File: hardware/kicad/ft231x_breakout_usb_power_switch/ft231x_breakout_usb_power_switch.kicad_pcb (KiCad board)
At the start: 2 copper layers, 60 x 31.2 mm, 48 parts, among them J1 USB_B_Micro_ALT, J2 USB_A_ALT, J4 Conn_01x04, SW1 PTS810SJK250SMTRLFS, U1 SRV05-4, U2 FT231XS, U3 TPS2553DBVR, U4 SN74LVC3G04DCTR, U5 NC7SZ66M5X

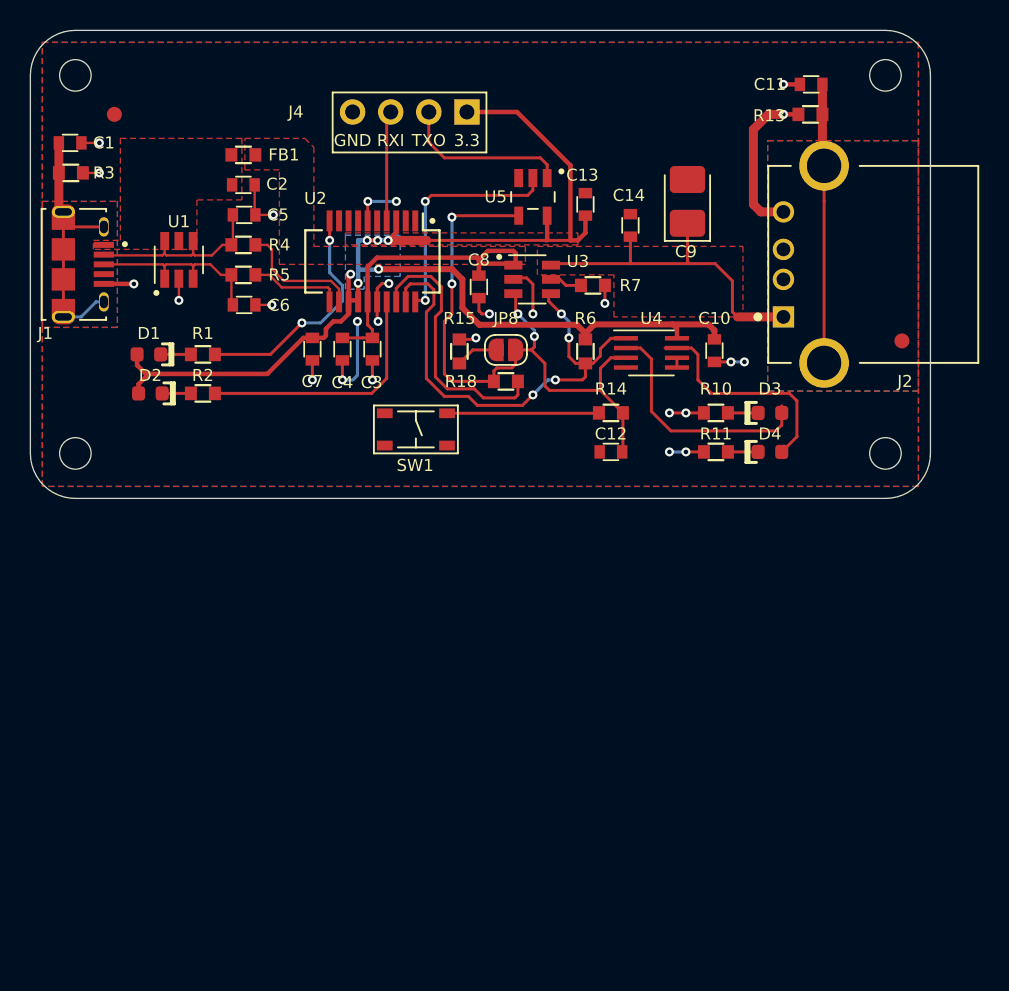
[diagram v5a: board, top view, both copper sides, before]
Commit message: 0.3-rc1 removed breakout headers
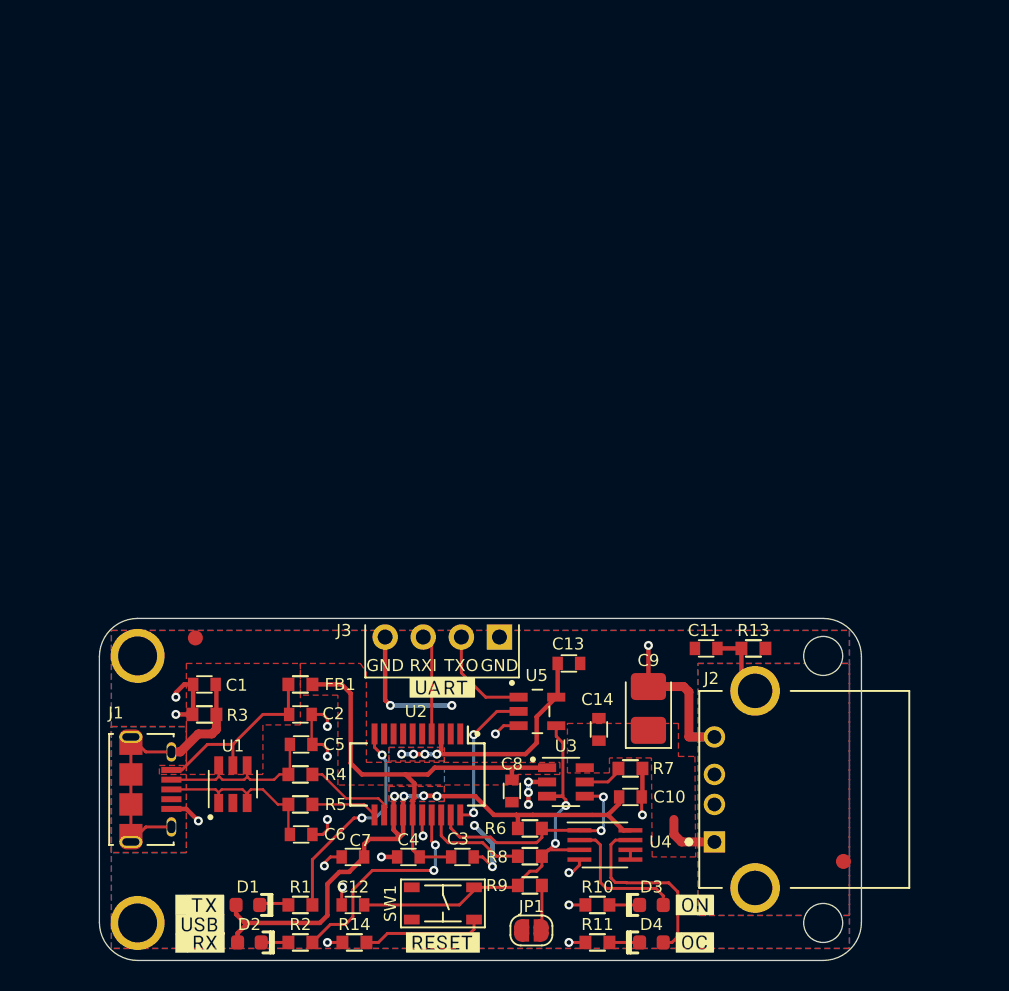
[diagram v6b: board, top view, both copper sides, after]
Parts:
- removed JP8: SolderJumper_2_Bridged_Alt, -Jumper:SolderJumper-2_P1.3mm_Un-Bridged_RoundedPad1.0x1.5mm
- removed R15: 10k, -Passive:R_0603
- removed R18: 5k1, -Passive:R_0603
- added ?: , buzzard_labels, F.Cu at (121.7, 130.2)
- added ?: , buzzard_labels, F.Cu at (121.7, 127.7)
- added ?: , buzzard_labels, F.Cu at (137.5, 130.2)
- added ?: , buzzard_labels, F.Cu at (137.5, 113.2)
- added ?: , buzzard_labels, F.Cu at (121.3, 129.0)
- added ?: , buzzard_labels, F.Cu at (154.3, 127.7)
- added ?: , buzzard_labels, F.Cu at (154.3, 130.2)
- added JP1: SolderJumper_2_Bridged_Alt, -Jumper:SolderJumper-2_P1.3mm_Un-Bridged_RoundedPad1.0x1.5mm, F.Cu at (143.4, 129.4)
- added R8: 5k1, -Passive:R_0603, F.Cu at (143.3, 124.5)
- added R9: 10k, -Passive:R_0603, F.Cu at (143.3, 126.4)
- H1, H3: footprint -Connector:MountingHole_2.1mm -> -Connector:MountingHole_2.6mm_annular
- H2, H4: footprint -Connector:MountingHole_2.1mm -> -Connector:MountingHole_2.6mm_nocrtyd
- moved R14 39.2 mm to (131.6, 130.2)
- moved H1 38.9 mm to (117.2, 111.1)
- moved H2 38.9 mm to (162.8, 111.1)
- moved C11 38.2 mm to (155.1, 110.6)
- moved D1 37.3 mm to (124.5, 127.7)
- moved R1 37.3 mm to (128.0, 127.7)
- moved C1 37.2 mm to (121.6, 113.0), turned to 180 degrees
- moved D2 37.2 mm to (124.6, 130.2)
- moved R3 37.2 mm to (121.6, 115.0), turned to 0 degrees
- moved R2 37.2 mm to (128.0, 130.2)
- moved R13 35.8 mm to (158.2, 110.6), turned to 180 degrees
- moved C2 35.5 mm to (128.0, 115.0)
- moved C5 35.5 mm to (128.1, 117.0)
- moved C6 35.5 mm to (128.1, 123.0)
- moved FB1 35.5 mm to (128.0, 113.0)
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- renumbered J4 to J3
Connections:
- J3 pad 1: +3V3 -> GND
- R14 pad 1: Net-(R14-Pad1) -> GND
- R14 pad 2: /EN -> Net-(R14-Pad2)
- SW1 pad 1: GND -> Net-(R14-Pad2)
- SW1 pad 3: Net-(R14-Pad1) -> /EN
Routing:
- net +3V3: track 88.0 -> 58.8 mm, vias 6 -> 8
- net Net-(C14-Pad1): track 23.9 -> 5.66 mm
- net /FAULT: track 32.2 -> 15.7 mm, vias 4 -> 2
- net /EN: track 42.4 -> 28.0 mm, vias 4 -> 2
- net Net-(C11-Pad1): track 18.6 -> 4.81 mm
- net Net-(C2-Pad1): track 0.00 -> 12.8 mm
- net /GPO: track 17.8 -> 7.06 mm
- net Net-(R14-Pad1): track 10.2 -> 0.00 mm
- net Net-(C3-Pad1): track 21.6 -> 29.9 mm
- net Net-(R14-Pad2): track 0.00 -> 8.26 mm
- net Net-(D3-Pad2): track 16.3 -> 10.1 mm
- net /TXD: track 15.6 -> 9.79 mm
- net GND: track 51.4 -> 57.0 mm, vias 26 -> 24
- net /STXD: track 11.4 -> 6.88 mm
- net Net-(JP1-Pad1): track 0.00 -> 3.32 mm
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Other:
- board size 60 x 31.2 mm -> 50.8 x 22.8 mm
- board text added: "Short JP1 to default USB power to off."
- board text added: "ft231x_uart_usb_power_switch"
- board text added: "v0.3<<hash>>"
- board text removed: "Short JP8 to default USB power to off."
- board text removed: "ft231x_breakout_usb_power_switch"
- board text removed: "v0.2<<hash>>"

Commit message: 0.3 rc2 fix zone fills
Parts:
- moved C11 0.10 mm to (155.1, 110.7)
- moved R13 0.10 mm to (158.2, 110.7)
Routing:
- net GND: track 57.0 -> 57.6 mm, vias 24 -> 25

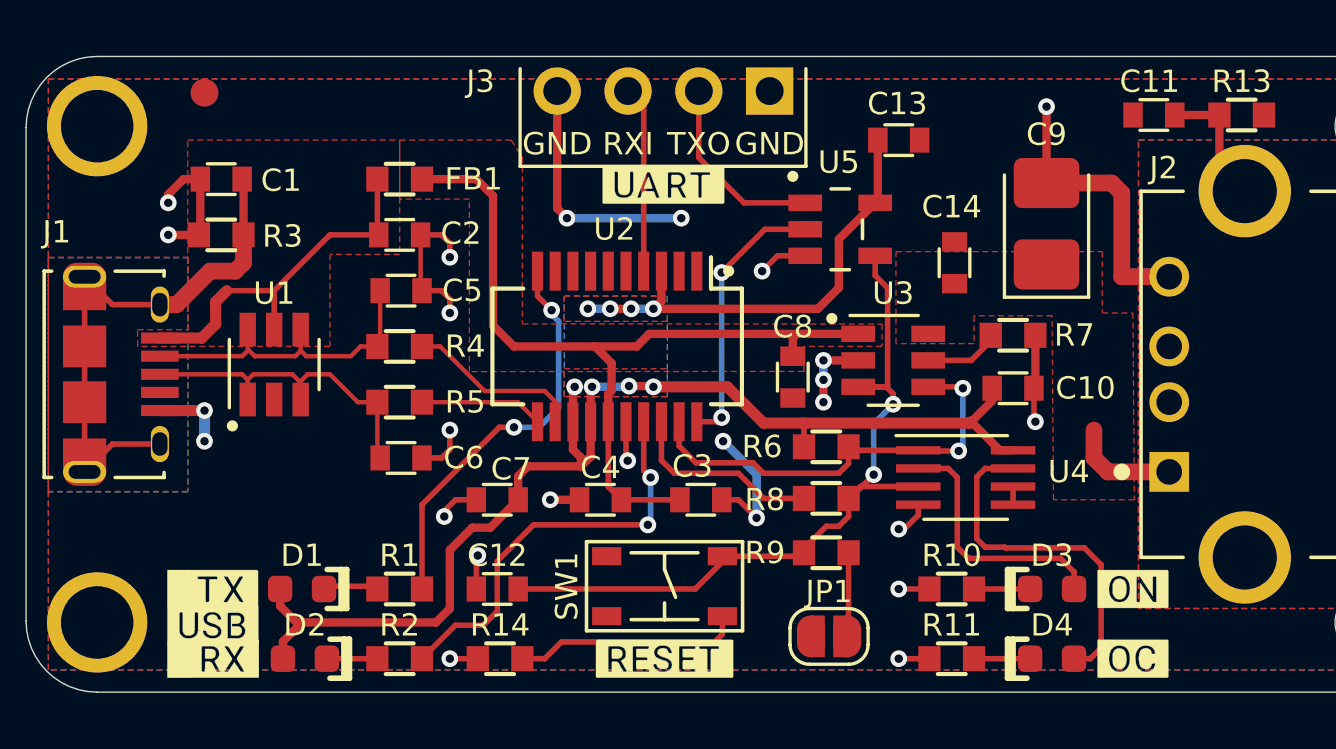
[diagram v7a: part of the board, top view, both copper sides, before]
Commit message: Add open hardware logos
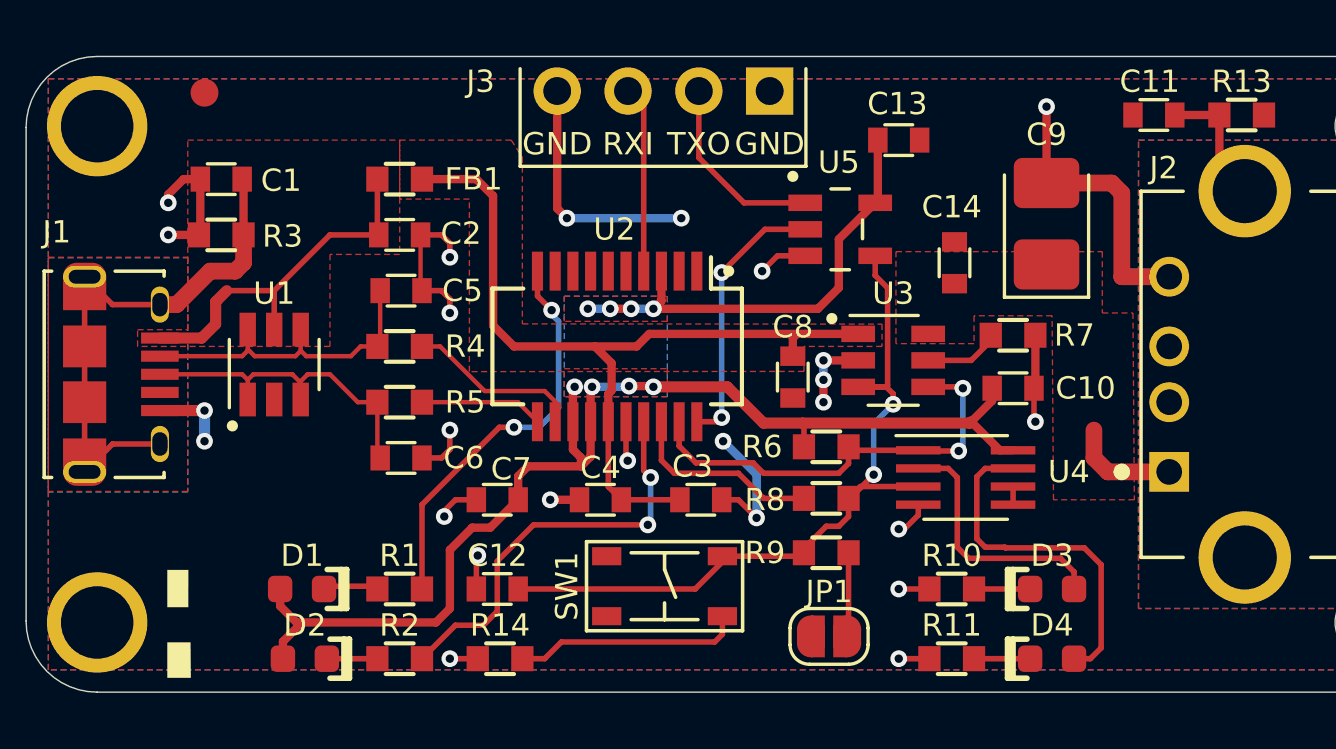
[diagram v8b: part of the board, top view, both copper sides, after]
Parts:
- removed ? (x7): , buzzard_labels
- added LOGO1: Logo_Open_Hardware_Small, -Logo:OSHW-Logo2_7.3x6mm_SilkScreen, B.Cu at (131.7, 126.5)
- added LOGO2: Logo_CC_BY_SA, -Logo:cc_by_sa, B.Cu at (144.1, 126.5)
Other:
- board text added: "github.com/paulsykes/ ft231x_breakout_usb_power_switch"
- board text removed: "ft231x_uart_usb_power_switch"
